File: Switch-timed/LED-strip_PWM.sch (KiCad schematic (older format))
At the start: 16 parts, among them IC1 ATTINY13A-MM, P1 CONN_2, P2 CONN_2, T1 AO3400, U1 MCP6001, U2 MCP1804-SOT23-5

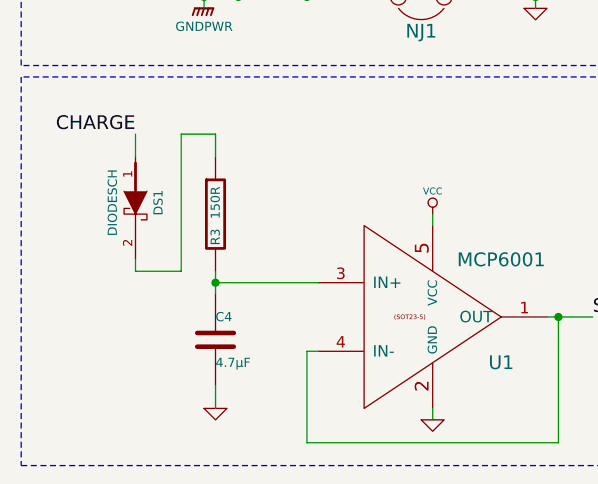
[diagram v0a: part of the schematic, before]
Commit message: Switch-timed: forgot RC-timer resistor + added BAT54.
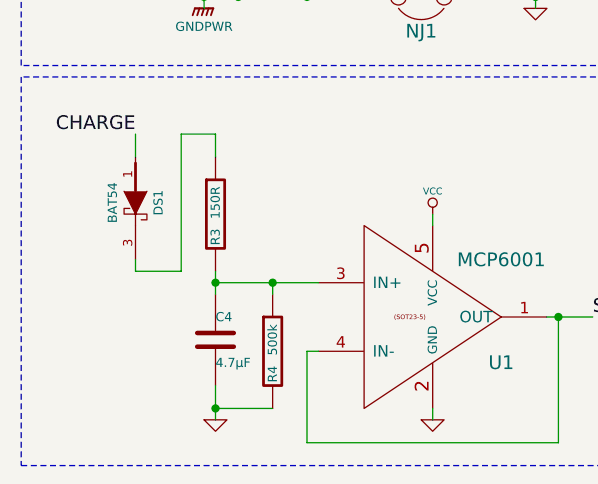
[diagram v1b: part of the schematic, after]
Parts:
- removed DS1: DIODESCH, ~, symbol DIODESCH
- added DS1: BAT54, symbol MADW__BAT54
- added R4: 500k, symbol R
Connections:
- net CHARGE: now also DS1.1 (A)
- net GND: now also R4.2
- net at C4.1, R3.2, U1.3 (IN+): now also R4.1
- net at R3.1: now also DS1.3 (C)
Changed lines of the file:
@@
 Text Notes 2700 775  0    39   ~ 0
 (MLF-10)
-$Comp
-L DIODESCH DS1
-U 1 1 519FC2B2
-P 1050 3600
-F 0 "DS1" H 1050 3700 40  0000 C CNN
-F 1 "DIODESCH" H 1050 3500 40  0000 C CNN
-F 2 "~" H 1050 3600 60  0000 C CNN
-F 3 "~" H 1050 3600 60  0000 C CNN
-	1    1050 3600
-	0    1    1    0
-$EndComp
 Text Label 950  1300 2    60   ~ 0
 CHARGE
@@
 L GND #PWR015
 U 1 1 519FC534
-P 1400 4500
-F 0 "#PWR015" H 1400 4500 30  0001 C CNN
-F 1 "GND" H 1400 4430 30  0001 C CNN
-F 2 "" H 1400 4500 60  0000 C CNN
-F 3 "" H 1400 4500 60  0000 C CNN
-	1    1400 4500
+P 1400 4550
+F 0 "#PWR015" H 1400 4550 30  0001 C CNN
+F 1 "GND" H 1400 4480 30  0001 C CNN
+F 2 "" H 1400 4550 60  0000 C CNN
+F 3 "" H 1400 4550 60  0000 C CNN
+	1    1400 4550
 	1    0    0    -1
 $EndComp
@@
 	1400 3900 1400 4000
 Wire Wire Line
-	1400 4400 1400 4500
+	1400 4400 1400 4550
 Wire Wire Line
 	1400 3950 1850 3950
@@
 Wire Notes Line
 	3400 3050 550  3050
+$Comp
+L R R4
+U 1 1 51A0D0CA
+P 1650 4250
+F 0 "R4" V 1650 4150 40  0000 C CNN
+F 1 "500k" V 1650 4300 40  0000 C CNN
+F 2 "" V 1580 4250 30  0000 C CNN
+F 3 "" H 1650 4250 30  0000 C CNN
+	1    1650 4250
+	1    0    0    -1
+$EndComp
+Wire Wire Line
+	1650 4000 1650 3950
+Connection ~ 1650 3950
+Wire Wire Line
+	1400 4500 1650 4500
+Connection ~ 1400 4500
+$Comp
+L MADW__BAT54 DS1
+U 1 1 51A0D7F5
+P 1050 3600
+F 0 "DS1" H 1050 3700 40  0000 C CNN
+F 1 "BAT54" H 1050 3500 40  0000 C CNN
+F 2 "" H 1050 3600 60  0000 C CNN
+F 3 "" H 1050 3600 60  0000 C CNN
+	1    1050 3600
+	0    1    1    0
+$EndComp
 $EndSCHEMATC

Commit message: Changed to custom attiny13 schematic symbol + footprint.
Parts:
- removed IC1: ATTINY13A-MM, QFN/MLF10, symbol ATTINY13A-MM
- added IC1: MADW__ATTINY13-MM, MADW__MLF10, symbol MADW__ATTINY13-MM
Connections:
- net CHARGE: now also IC1.4 (PB4(ADC2/PCINT4))
- net GND: now also IC1.5 (GND), IC1.PAD (GND)
- net MISO: now also IC1.7 (PB1(MISO/AIN1/OC0B/INT0/PCINT1))
- net MOSI: now also IC1.6 (PB0(MOSI/AIN0/OC0A/PCINT0))
- net RESET: now also IC1.1 (PB5(~RESET~/ADC0/PCINT5/dW))
- net SCK: now also IC1.9 (PB2(SCK/ADC1/T0/PCINT2))
- net SENSE: now also IC1.2 (PB3(CLKI/ADC3/PCINT3))
- net VCC: now also IC1.10 (VCC)
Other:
- note removed: "(MLF-10)"
- moved on the sheet: C1, JP1
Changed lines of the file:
@@
-$EndComp
-$Comp
-L C C1
-U 1 1 4F76EBA8
-P 3300 1150
-F 0 "C1" H 3350 1250 50  0000 L CNN
-F 1 "100nF" H 3350 1050 50  0000 L CNN
-F 2 "" H 3300 1150 60  0001 C CNN
-F 3 "" H 3300 1150 60  0001 C CNN
-	1    3300 1150
-	1    0    0    -1
 $EndComp
 $Comp
@@
 L VCC #PWR02
 U 1 1 4F6EE887
-P 3300 900
-F 0 "#PWR02" H 3300 1000 30  0001 C CNN
-F 1 "VCC" H 3300 1000 30  0000 C CNN
-F 2 "" H 3300 900 60  0001 C CNN
-F 3 "" H 3300 900 60  0001 C CNN
-	1    3300 900
+P 3350 900
+F 0 "#PWR02" H 3350 1000 30  0001 C CNN
+F 1 "VCC" H 3350 1000 30  0000 C CNN
+F 2 "" H 3350 900 60  0001 C CNN
+F 3 "" H 3350 900 60  0001 C CNN
+	1    3350 900
 	1    0    0    -1
 $EndComp
@@
 L GND #PWR03
 U 1 1 4F6EE882
-P 3300 1450
-F 0 "#PWR03" H 3300 1450 30  0001 C CNN
-F 1 "GND" H 3300 1380 30  0001 C CNN
-F 2 "" H 3300 1450 60  0001 C CNN
-F 3 "" H 3300 1450 60  0001 C CNN
-	1    3300 1450
+P 3350 1450
+F 0 "#PWR03" H 3350 1450 30  0001 C CNN
+F 1 "GND" H 3350 1380 30  0001 C CNN
+F 2 "" H 3350 1450 60  0001 C CNN
+F 3 "" H 3350 1450 60  0001 C CNN
+	1    3350 1450
 	1    0    0    -1
 $EndComp
@@
 L GND #PWR04
 U 1 1 4F6EE81E
-P 4800 1300
-F 0 "#PWR04" H 4800 1300 30  0001 C CNN
-F 1 "GND" H 4800 1230 30  0001 C CNN
-F 2 "" H 4800 1300 60  0001 C CNN
-F 3 "" H 4800 1300 60  0001 C CNN
-	1    4800 1300
-	1    0    0    -1
-$EndComp
-Text Label 4800 1150 0    60   ~ 0
+P 4850 1300
+F 0 "#PWR04" H 4850 1300 30  0001 C CNN
+F 1 "GND" H 4850 1230 30  0001 C CNN
+F 2 "" H 4850 1300 60  0001 C CNN
+F 3 "" H 4850 1300 60  0001 C CNN
+	1    4850 1300
+	1    0    0    -1
+$EndComp
+Text Label 4850 1150 0    60   ~ 0
 MOSI
 $Comp
 L VCC #PWR05
 U 1 1 4F6EE80A
-P 4800 1050
-F 0 "#PWR05" H 4800 1150 30  0001 C CNN
-F 1 "VCC" H 4800 1150 30  0000 C CNN
-F 2 "" H 4800 1050 60  0001 C CNN
-F 3 "" H 4800 1050 60  0001 C CNN
-	1    4800 1050
-	1    0    0    -1
-$EndComp
-Text Label 3900 1250 2    60   ~ 0
+P 4850 1050
+F 0 "#PWR05" H 4850 1150 30  0001 C CNN
+F 1 "VCC" H 4850 1150 30  0000 C CNN
+F 2 "" H 4850 1050 60  0001 C CNN
+F 3 "" H 4850 1050 60  0001 C CNN
+	1    4850 1050
+	1    0    0    -1
+$EndComp
+Text Label 3950 1250 2    60   ~ 0
 RESET
-Text Label 3900 1150 2    60   ~ 0
+Text Label 3950 1150 2    60   ~ 0
 SCK
-Text Label 3900 1050 2    60   ~ 0
+Text Label 3950 1050 2    60   ~ 0
 MISO
 $Comp
 L MADW__AVR_ISP JP1
 U 1 1 4F6EC6BB
-P 4350 1150
-F 0 "JP1" H 4300 1350 50  0000 L BNN
-F 1 "ISP" H 4300 850 50  0000 L BNN
-F 2 "" H 4350 1150 60  0001 C CNN
-F 3 "" H 4350 1150 60  0001 C CNN
-	1    4350 1150
+P 4400 1150
+F 0 "JP1" H 4350 1350 50  0000 L BNN
+F 1 "ISP" H 4350 850 50  0000 L BNN
+F 2 "" H 4400 1150 60  0001 C CNN
+F 3 "" H 4400 1150 60  0001 C CNN
+	1    4400 1150
 	1    0    0    -1
 $EndComp
@@
 $EndComp
 $Comp
-L ATTINY13A-MM IC1
-U 1 1 519FBED0
-P 1400 800
-F 0 "IC1" H 1500 850 60  0000 C CNN
-F 1 "ATTINY13A-MM" H 2700 50  60  0000 C CNN
-F 2 "QFN/MLF10" H 1700 50  60  0001 C CNN
-F 3 "~" H 1400 800 60  0000 C CNN
-	1    1400 800
-	1    0    0    -1
-$EndComp
-$Comp
 L MOSFET_N T1
 U 1 1 519FBEE4
@@
 Text Label 950  1200 2    60   ~ 0
 SENSE
-Text Notes 2700 775  0    39   ~ 0
-(MLF-10)
 Text Label 950  1300 2    60   ~ 0
 CHARGE
@@
 $EndComp
 Wire Wire Line
-	3300 950  3300 900
-Wire Wire Line
-	3300 900  3200 900
-Wire Wire Line
-	4800 1300 4800 1250
-Wire Wire Line
-	4800 1250 4650 1250
-Wire Wire Line
-	4650 1050 4800 1050
-Wire Wire Line
-	4050 1150 3900 1150
-Wire Wire Line
-	4050 1050 3900 1050
-Wire Wire Line
-	4050 1250 3900 1250
-Wire Wire Line
-	4650 1150 4800 1150
-Wire Wire Line
-	3300 1400 3200 1400
-Wire Wire Line
-	3300 1350 3300 1450
-Connection ~ 3300 1400
+	3200 900  3350 900
+Wire Wire Line
+	4850 1300 4850 1250
+Wire Wire Line
+	4850 1250 4700 1250
+Wire Wire Line
+	4700 1050 4850 1050
+Wire Wire Line
+	4100 1150 3950 1150
+Wire Wire Line
+	4100 1050 3950 1050
+Wire Wire Line
+	4100 1250 3950 1250
+Wire Wire Line
+	4700 1150 4850 1150
 Wire Wire Line
 	4850 2650 4850 2800
@@
 	0    1    1    0
 $EndComp
+$Comp
+L C C1
+U 1 1 4F76EBA8
+P 3350 1150
+F 0 "C1" H 3400 1250 50  0000 L CNN
+F 1 "100nF" H 3400 1050 50  0000 L CNN
+F 2 "" H 3350 1150 60  0001 C CNN
+F 3 "" H 3350 1150 60  0001 C CNN
+	1    3350 1150
+	1    0    0    -1
+$EndComp
+Wire Wire Line
+	3350 900  3350 950
+Wire Wire Line
+	3350 1350 3350 1450
+Wire Wire Line
+	3200 1300 3250 1300
+Wire Wire Line
+	3250 1300 3250 1400
+Wire Wire Line
+	3250 1400 3200 1400
+Wire Wire Line
+	3250 1350 3350 1350
+Connection ~ 3250 1350
+$Comp
+L MADW__ATTINY13-MM IC1
+U 1 1 51B1F092
+P 2200 1150
+F 0 "IC1" H 1500 1550 60  0000 C CNN
+F 1 "MADW__ATTINY13-MM" H 2550 750 60  0000 C CNN
+F 2 "MADW__MLF10" H 1700 750 60  0000 C CNN
+F 3 "" H 1400 1500 60  0000 C CNN
+	1    2200 1150
+	1    0    0    -1
+$EndComp
 $EndSCHEMATC

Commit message: Switch-timed: switched to ATtiny10 SOT23-6.
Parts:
- removed IC1: MADW__ATTINY13-MM, MADW__MLF10, symbol MADW__ATTINY13-MM
- removed JP1: ISP, symbol MADW__AVR_ISP
- added IC1: ATTINY10-TS, SOT23-6, symbol ATTINY10-TS
- added JP1: MADW__AVR_TPI, symbol MADW__AVR_TPI
- added R5: 1k, symbol R
- R3: value 150R -> 1k
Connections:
- net CHARGE: now also IC1.4 (PB2(INT0/ADC2/T0/PCINT2/CLKO))
- net GND: now also IC1.2 (GND), JP1.6 (GND)
- net RESET: now also IC1.6 (PB3(~RESET~/ADC3/PCINT3)), JP1.5 (RST)
- net SENSE: now also IC1.3 (PB1(AIN1/ADC1/OC0B/ICP0/PCINT1/CLKI/TPICLK)), JP1.3 (SCK), R5.2; no longer U1.1 (OUT), U1.4 (IN-)
- net VCC: now also IC1.5 (VCC), JP1.2 (VTG)
- net MOSI renamed GATE
- net GATE: now also IC1.1 (PB0(AIN0/ADC0/OC0A/PCINT0/TPIDATA)), JP1.1 (DATA)
- new net: R5.1, U1.1 (OUT), U1.4 (IN-)
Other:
- moved on the sheet: C1

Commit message: Revert "Switch-timed: switched to ATtiny10 SOT23-6."
This reverts commit 7426c306dc58e77c9809db77e26f6b62b76c1d9c.

C + ATtiny10 not supported by avr-gcc
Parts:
- removed IC1: ATTINY10-TS, SOT23-6, symbol ATTINY10-TS
- removed JP1: MADW__AVR_TPI, symbol MADW__AVR_TPI
- removed R5: 1k, symbol R
- added IC1: MADW__ATTINY13-MM, MADW__MLF10, symbol MADW__ATTINY13-MM
- added JP1: ISP, symbol MADW__AVR_ISP
- R3: value 1k -> 150R
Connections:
- net CHARGE: now also IC1.4 (PB4(ADC2/PCINT4))
- net GND: now also IC1.5 (GND), IC1.PAD (GND), JP1.6 (GND)
- net RESET: now also IC1.1 (PB5(~RESET~/ADC0/PCINT5/dW)), JP1.5 (RST)
- net SENSE: now also U1.1 (OUT), U1.4 (IN-), IC1.2 (PB3(CLKI/ADC3/PCINT3))
- net VCC: now also IC1.10 (VCC), JP1.2 (VTG)
- net GATE renamed MOSI
- net MOSI: now also IC1.6 (PB0(MOSI/AIN0/OC0A/PCINT0)), JP1.4 (MOSI)
- new net MISO: IC1.7 (PB1(MISO/AIN1/OC0B/INT0/PCINT1)), JP1.1 (MISO)
- new net SCK: IC1.9 (PB2(SCK/ADC1/T0/PCINT2)), JP1.3 (SCK)
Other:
- moved on the sheet: C1
